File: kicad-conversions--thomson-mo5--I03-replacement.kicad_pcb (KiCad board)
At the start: 2 copper layers, 15.9 x 29.8 mm, 3 parts, among them U1 HM7603_32×8_PROM_THREE-STATE_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, U2 HIGH_PERFORMANCE_E2_CMOS_PLD_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

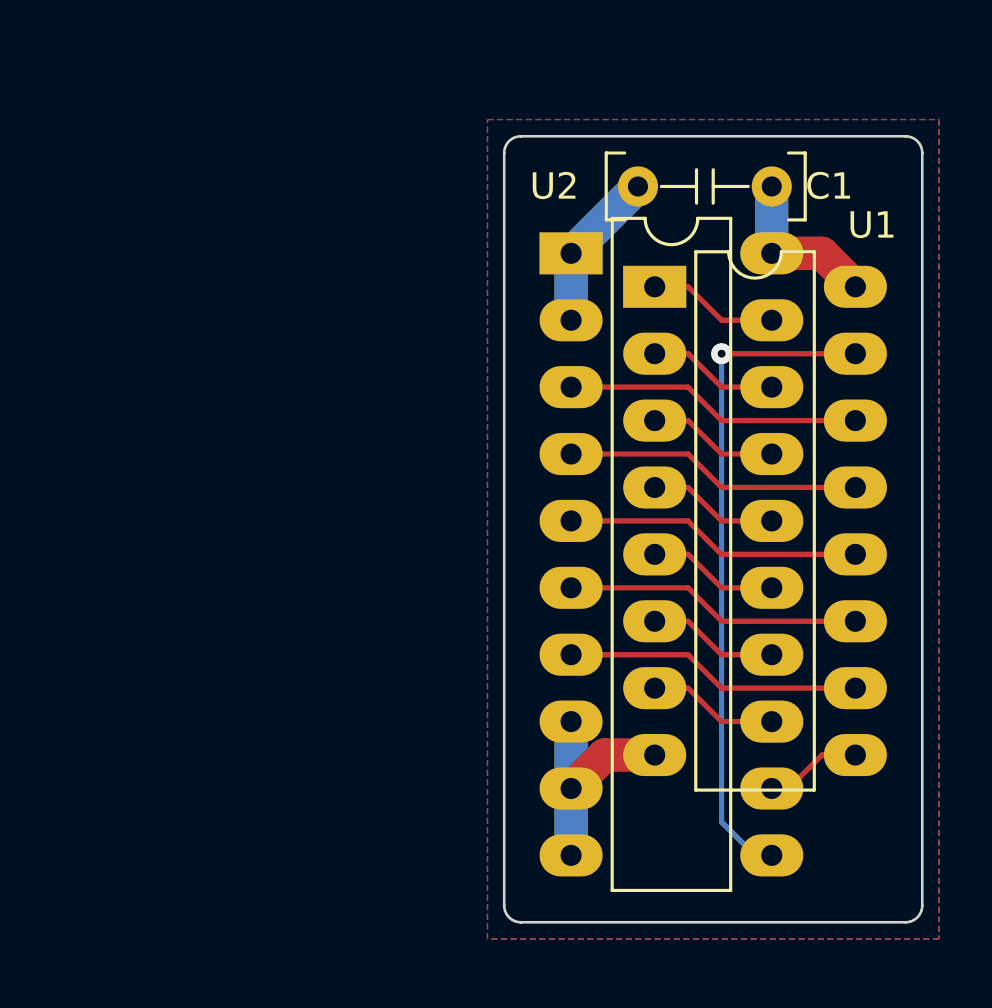
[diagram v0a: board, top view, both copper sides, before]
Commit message: Resolves #6 : Add a breakout connector with R[1..2], V[1..2] and B[1..2] for adding custom DAC mods
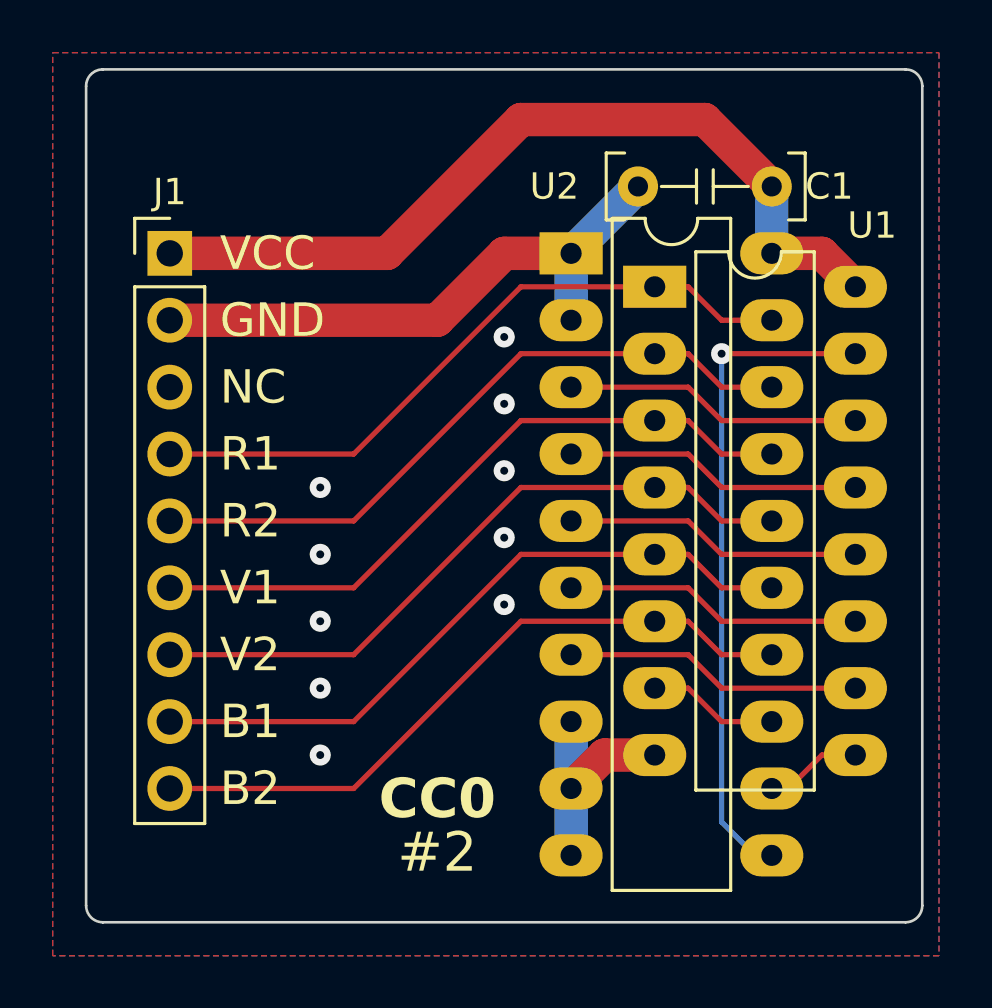
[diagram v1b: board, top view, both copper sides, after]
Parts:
- added J1: RVB DAC, Connector_PinHeader_2.54mm:PinHeader_1x09_P2.54mm_Vertical, F.Cu at (57.8, 74.9)
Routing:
- net /VCC: track 6.24 -> 32.3 mm
- net /V2: track 4.97 -> 26.0 mm
- net /R2: track 4.97 -> 26.0 mm
- net /V1: track 4.97 -> 26.0 mm
- net /R1: track 4.97 -> 26.0 mm
- net /B2: track 4.97 -> 26.0 mm
- net /B1: track 4.97 -> 26.0 mm
- net /GND: track 14.9 -> 31.2 mm, vias 0 -> 10
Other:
- board size 15.9 x 29.8 mm -> 31.8 x 32.4 mm
- board text added: "B1"
- board text added: "B2"
- board text added: "GND"
- board text added: "NC"
- board text added: "R1"
- board text added: "R2"
- board text added: "V1"
- board text added: "V2"
- board text added: "VCC"
